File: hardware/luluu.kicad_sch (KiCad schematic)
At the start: 53 parts, among them J1 BATT_CON, J2 RPi SWD, J3 STEMMA_{QT} I_{2}C, J4 Micro_SD_Card, J5 RPi UART, J6 USB_C_Receptacle_USB2.0, J7 DISP_LCD_ST7789, Q1 AO3401A, Q2 BSS138, SW1 SW_USBBOOT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

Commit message: design rules
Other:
- company: (none) -> Gray Olson
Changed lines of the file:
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@@
   (title_block
     (title "LuLuu")
+    (date "2023-10-13")
     (rev "0")
+    (company "Gray Olson")
+    (comment 1 "Made with love by")
+    (comment 2 "A cute and smart arm warmer sleeve ^_^")
   )
   (junction (at 100.33 39.37) (diameter 0) (color 0 0 0 0)
@@
   (junction (at 254 140.97) (diameter 0) (color 0 0 0 0)
   )
+  (junction (at 267.97 48.26) (diameter 0) (color 0 0 0 0)
+  )
   (junction (at 39.37 153.67) (diameter 0) (color 0 0 0 0)
   )
@@
   (junction (at 24.13 102.87) (diameter 0) (color 0 0 0 0)
   )
-  (junction (at 267.97 40.64) (diameter 0) (color 0 0 0 0)
-  )
   (junction (at 41.91 102.87) (diameter 0) (color 0 0 0 0)
   )
-  (junction (at 267.97 45.72) (diameter 0) (color 0 0 0 0)
-  )
   (junction (at 111.76 93.98) (diameter 0) (color 0 0 0 0)
   )
@@
   )
   (junction (at 119.38 68.58) (diameter 0) (color 0 0 0 0)
+  )
+  (junction (at 267.97 43.18) (diameter 0) (color 0 0 0 0)
   )
   (junction (at 149.86 83.82) (diameter 0) (color 0 0 0 0)
@@
     (stroke (width 0) (type default))
   )
-  (wire (pts (xy 267.97 45.72) (xy 269.24 45.72))
+  (wire (pts (xy 267.97 48.26) (xy 270.51 48.26))
     (stroke (width 0) (type default))
   )
@@
     (stroke (width 0) (type default))
   )
-  (wire (pts (xy 267.97 40.64) (xy 269.24 40.64))
+  (wire (pts (xy 267.97 43.18) (xy 270.51 43.18))
     (stroke (width 0) (type default))
   )
@@
     )
   )
-  (global_label "USB_D+" (shape bidirectional) (at 269.24 45.72 0) (fields_autoplaced)
-    (effects (font (size 1.27 1.27)) (justify left))
-    (property "Intersheetrefs" "${INTERSHEET_REFS}" (at 280.9565 45.72 0)
+  (global_label "USB_D+" (shape bidirectional) (at 270.51 48.26 0) (fields_autoplaced)
+    (effects (font (size 1.27 1.27)) (justify left))
+    (property "Intersheetrefs" "${INTERSHEET_REFS}" (at 282.2265 48.26 0)
       (effects (font (size 1.27 1.27)) (justify left) hide)
     )
@@
     )
   )
-  (global_label "USB_D-" (shape bidirectional) (at 269.24 40.64 0) (fields_autoplaced)
-    (effects (font (size 1.27 1.27)) (justify left))
-    (property "Intersheetrefs" "${INTERSHEET_REFS}" (at 280.9565 40.64 0)
+  (global_label "USB_D-" (shape bidirectional) (at 270.51 43.18 0) (fields_autoplaced)
+    (effects (font (size 1.27 1.27)) (justify left))
+    (property "Intersheetrefs" "${INTERSHEET_REFS}" (at 282.2265 43.18 0)
       (effects (font (size 1.27 1.27)) (justify left) hide)
     )
@@
     )
   )
+  (netclass_flag "" (length 2.54) (shape round) (at 270.51 48.26 0) (fields_autoplaced)
+    (effects (font (size 1.27 1.27)) (justify left bottom))
+    (property "Netclass" "USB Data" (at 271.2085 45.72 0)
+      (effects (font (size 1.27 1.27) italic) (justify left))
+    )
+  )
+  (netclass_flag "" (length 2.54) (shape round) (at 270.51 43.18 0) (fields_autoplaced)
+    (effects (font (size 1.27 1.27)) (justify left bottom))
+    (property "Netclass" "USB Data" (at 271.2085 40.64 0)
+      (effects (font (size 1.27 1.27) italic) (justify left))
+    )
+  )

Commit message: initial routing, various fixes
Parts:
- C12, C9: footprint Capacitor_SMD:C_0603_1608Metric_Pad1.08x0.95mm_HandSolder -> Capacitor_SMD:C_0402_1005Metric_Pad0.74x0.62mm_HandSolder; LCSC C15849 -> C52923
- SW1, SW2: symbol luluu:TS-1187A-B-A-B -> Switch:SW_Push
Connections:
- net +3V3: no longer SW1.
- net +BATT: now also SW3.2 (B); no longer J1.1 (Pin_1)
- net GND: now also J1.2 (Pin_2), SW1.2, SW2.1; no longer SW1., SW2., SW3.2 (B)
- net USBR_D-: now reaches R5.2, U3.47 (USB_DP)
- net at SW3.1 (A): now also J1.1 (Pin_1); no longer J1.2 (Pin_2)
- net at R7.1, U3.26 (RUN): now also SW2.2; no longer SW2.
- net USBR_D+: now reaches R6.2, U3.46 (USB_DM)
- net at R3.1, U1.1 (~{CS}), U3.56 (QSPI_SS): now also SW1.1
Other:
- title: LuLuu -> LuLuu!
- moved on the sheet: J1, R3, R5, R6, SW3

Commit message: update pwr switch silkscreen
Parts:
- SW3: footprint Button_Switch_SMD:SW_SPDT_PCM12 -> luluu:SW_SPDT_PCM12
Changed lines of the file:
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@@
       (effects (font (size 1.27 1.27)) (justify left))
     )
-    (property "Footprint" "Button_Switch_SMD:SW_SPDT_PCM12" (at 142.24 31.75 0)
+    (property "Footprint" "luluu:SW_SPDT_PCM12" (at 142.24 31.75 0)
       (effects (font (size 1.27 1.27)) hide)
     )

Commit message: initial prod
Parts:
- J1, J2, J3, J5, J7, SW3: now left out of the parts list
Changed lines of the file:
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@@
   )
   (symbol (lib_id "Connector_Generic:Conn_01x02") (at 148.59 38.1 0) (unit 1)
-    (in_bom yes) (on_board yes) (dnp no)
+    (in_bom no) (on_board yes) (dnp no)
     (property "Reference" "J1" (at 147.32 35.56 0)
       (effects (font (size 1.27 1.27)) (justify left))
@@
   )
   (symbol (lib_id "luluu:STEMMA_QT_I2C") (at 191.77 118.11 0) (mirror y) (unit 1)
-    (in_bom yes) (on_board yes) (dnp no)
+    (in_bom no) (on_board yes) (dnp no)
     (property "Reference" "J3" (at 198.12 116.84 0)
       (effects (font (size 1.27 1.27)))
@@
   )
   (symbol (lib_id "Connector_Generic:Conn_01x03") (at 195.58 151.13 0) (unit 1)
-    (in_bom yes) (on_board yes) (dnp no)
+    (in_bom no) (on_board yes) (dnp no)
     (property "Reference" "J2" (at 198.12 148.59 0)
       (effects (font (size 1.27 1.27)) (justify left))
@@
   )
   (symbol (lib_id "luluu:DISP_LCD_ST7789_1.3IN") (at 262.89 127 0) (unit 1)
-    (in_bom yes) (on_board yes) (dnp no)
+    (in_bom no) (on_board yes) (dnp no)
     (property "Reference" "J7" (at 257.81 93.98 0)
       (effects (font (size 1.27 1.27)) (justify left))
@@
   )
   (symbol (lib_id "Switch:SW_SPST") (at 142.24 31.75 270) (mirror x) (unit 1)
-    (in_bom yes) (on_board yes) (dnp no)
+    (in_bom no) (on_board yes) (dnp no)
     (property "Reference" "SW3" (at 144.78 33.02 90)
       (effects (font (size 1.27 1.27)) (justify left))
@@
   )
   (symbol (lib_id "Connector_Generic:Conn_01x03") (at 195.58 139.7 0) (unit 1)
-    (in_bom yes) (on_board yes) (dnp no)
+    (in_bom no) (on_board yes) (dnp no)
     (property "Reference" "J5" (at 198.12 137.16 0)
       (effects (font (size 1.27 1.27)) (justify left))

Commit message: layout improvements and jlcpcb part positioning offsets
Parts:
- J4, Q1, Q2, U5: JLCPCB Rotation Offset (none) -> 180
- J6: JLCPCB Position Offset (none) -> 0.0,1.25
- U1, U2, U4: JLCPCB Rotation Offset (none) -> -90
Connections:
- net GND: now also U3.19 (TESTEN)
- no-connect marks 25 -> 24
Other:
- note added: "Connector specified by Adafruit STEMMA_{QT} / SparkFun Qwiic"
- note added: "UART, I_{2}C and SPI Compatible with Adafruit Feather GPIO Layout"
- note removed: "Connector specified by Adafruit STEMMA_{QT}"

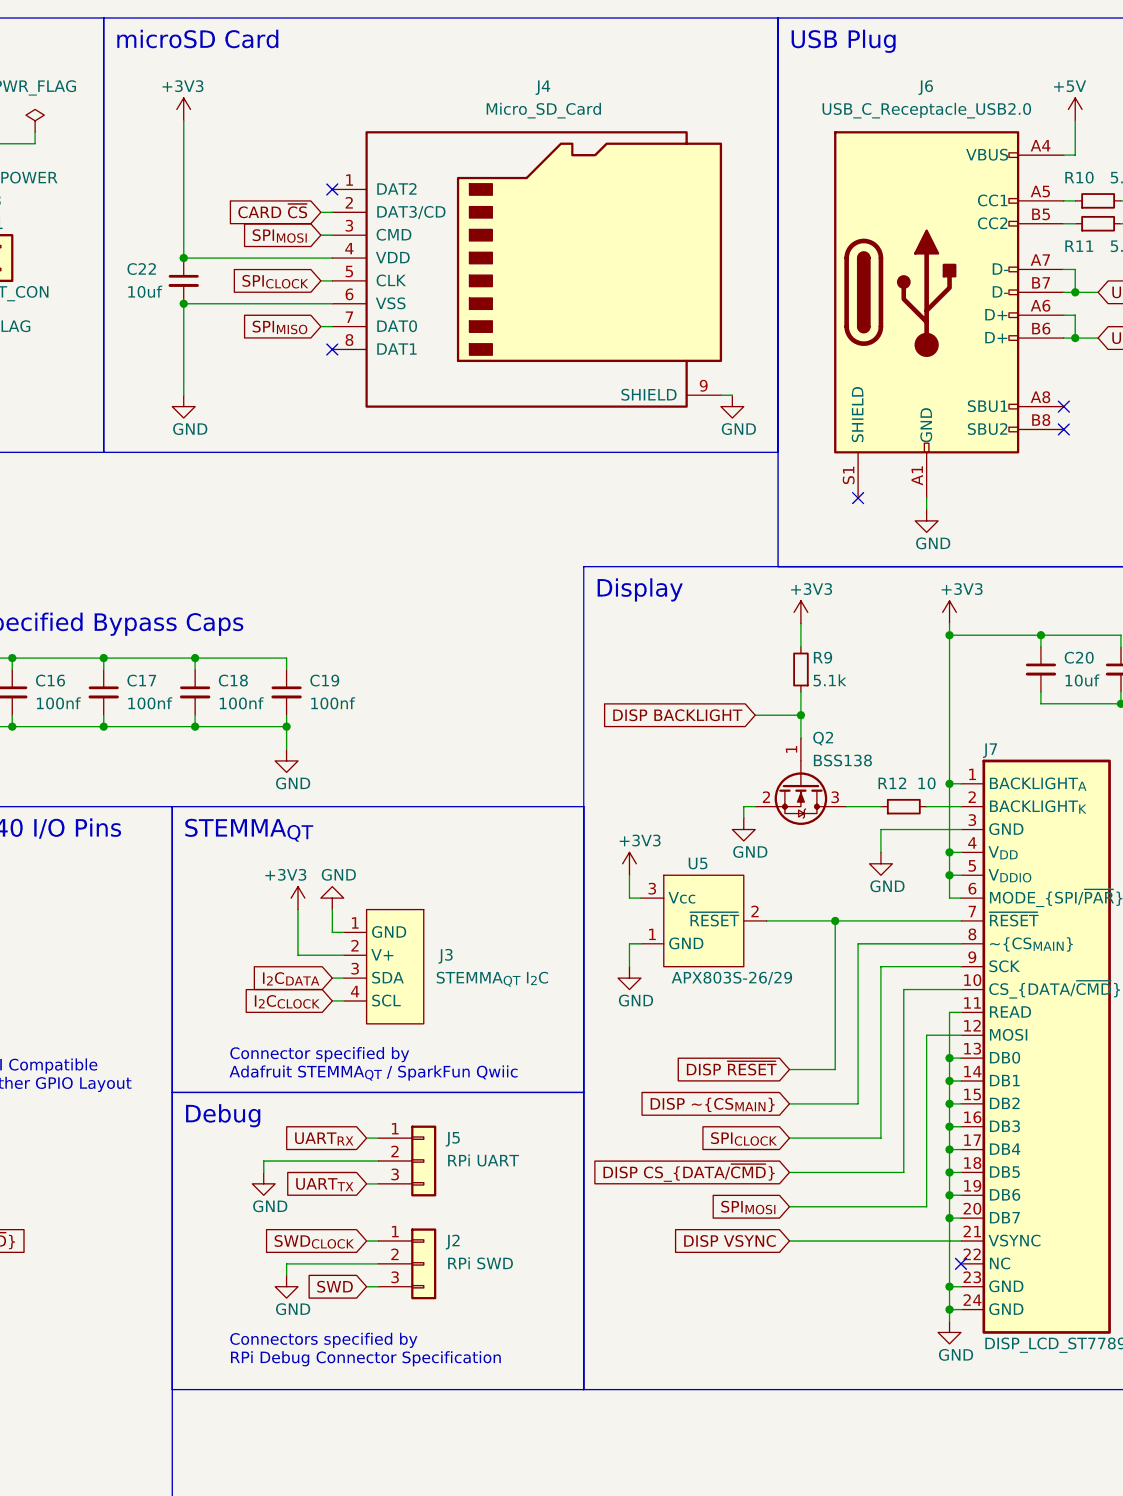
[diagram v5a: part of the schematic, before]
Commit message: add pullups to disp reset, disp csmain, card cs
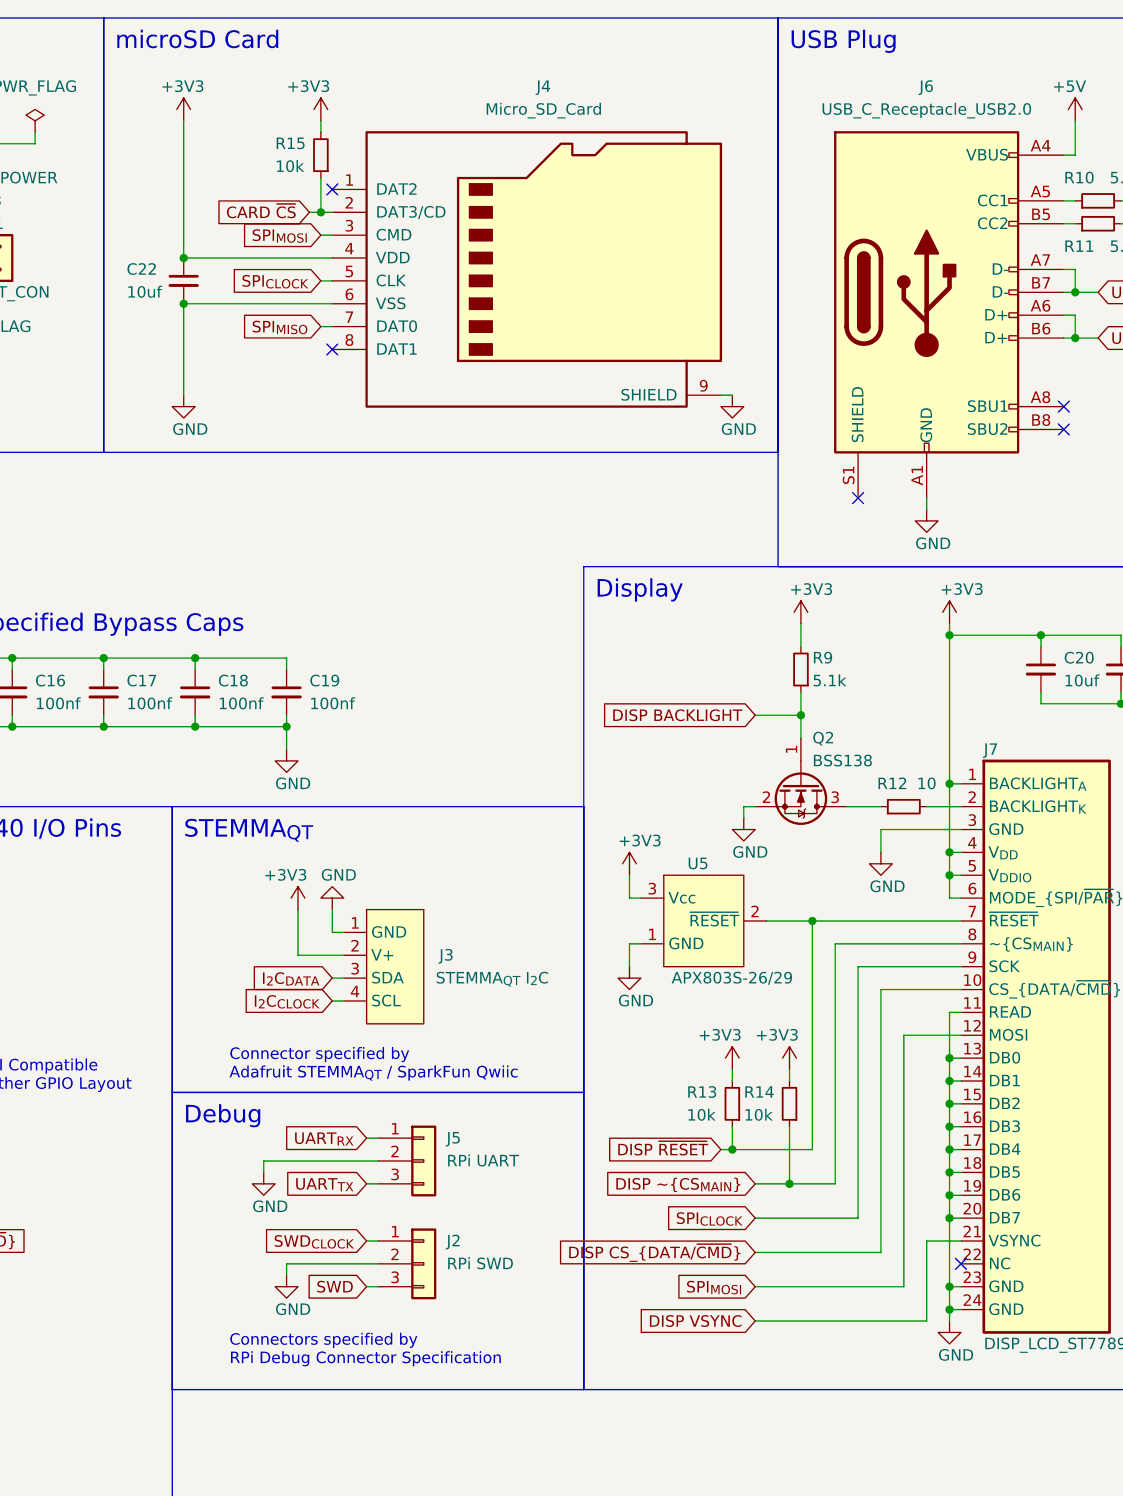
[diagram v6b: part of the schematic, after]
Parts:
- added R13, R14, R15: 10k, Resistor_SMD:R_0603_1608Metric_Pad0.98x0.95mm_HandSolder, symbol Device:R_Small
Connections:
- net +3V3: now also R13.2, R14.2, R15.2
- net CARD ~{CS}: now also R15.1
- net DISP ~{CS_{MAIN}}: now also R14.1
- net DISP ~{RESET}: now also R13.1

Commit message: change from farnell to digikey for other bom parts
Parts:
- J1: DigiKey (none) -> 455-S2B-PH-SM4-TBCT-ND; Farnell OC 9492615 -> (none)
- J2, J5: DigiKey (none) -> 455-BM03B-SRSS-TBCT-ND; Farnell OC 1679128 -> (none)
- J3: DigiKey (none) -> 455-SM04B-SRSS-TBCT-ND; Farnell OC 1830839 -> (none)
- J7: DigiKey (none) -> WM11305-ND; Farnell OC 3385226 -> (none)
- SW3: DigiKey (none) -> 401-2016-1-ND; Farnell OC 9575146 -> (none)
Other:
- note added: "UART & I_{2}C compatible with Adafruit Feather GPIO Layout"
- note removed: "UART, I_{2}C and SPI Compatible with Adafruit Feather GPIO Layout"
